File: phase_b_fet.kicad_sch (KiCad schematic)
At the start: 24 parts, among them Q6 IAUS300N08S5N0, Q7 IAUS300N08S5N0, Q8 IAUS300N08S5N0, Q9 IAUS300N08S5N0, U5 INA241A2

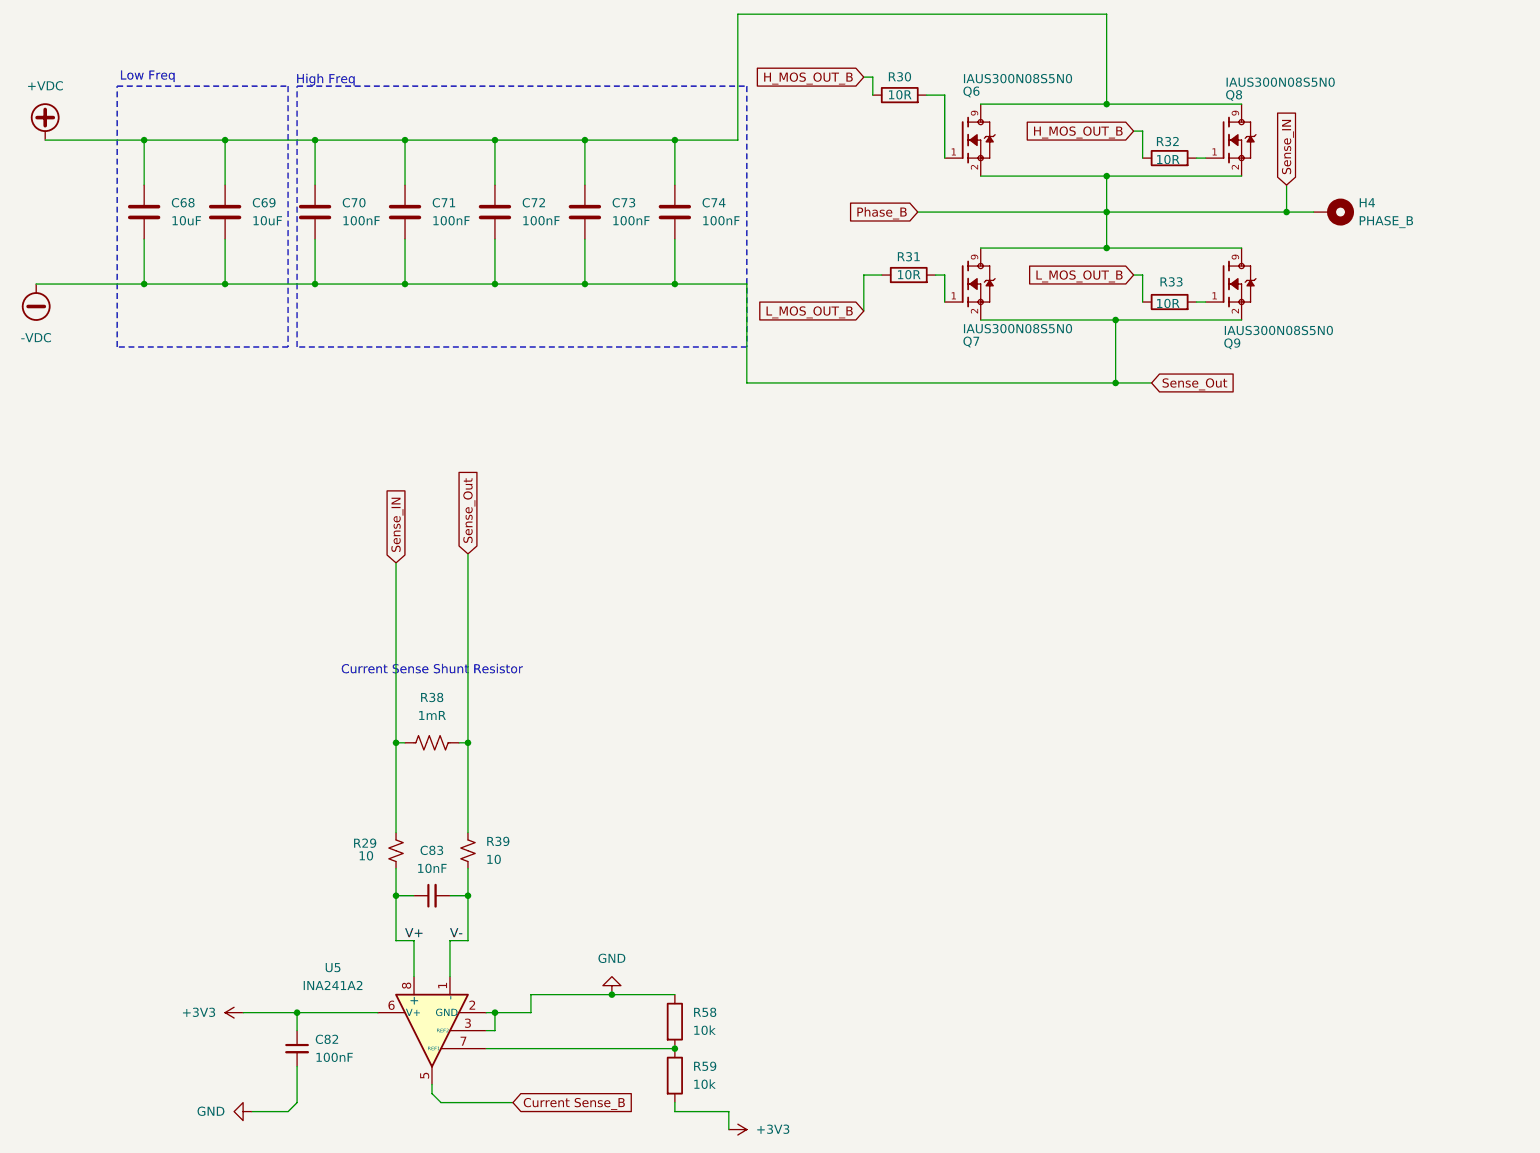
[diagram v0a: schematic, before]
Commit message: update: revised label
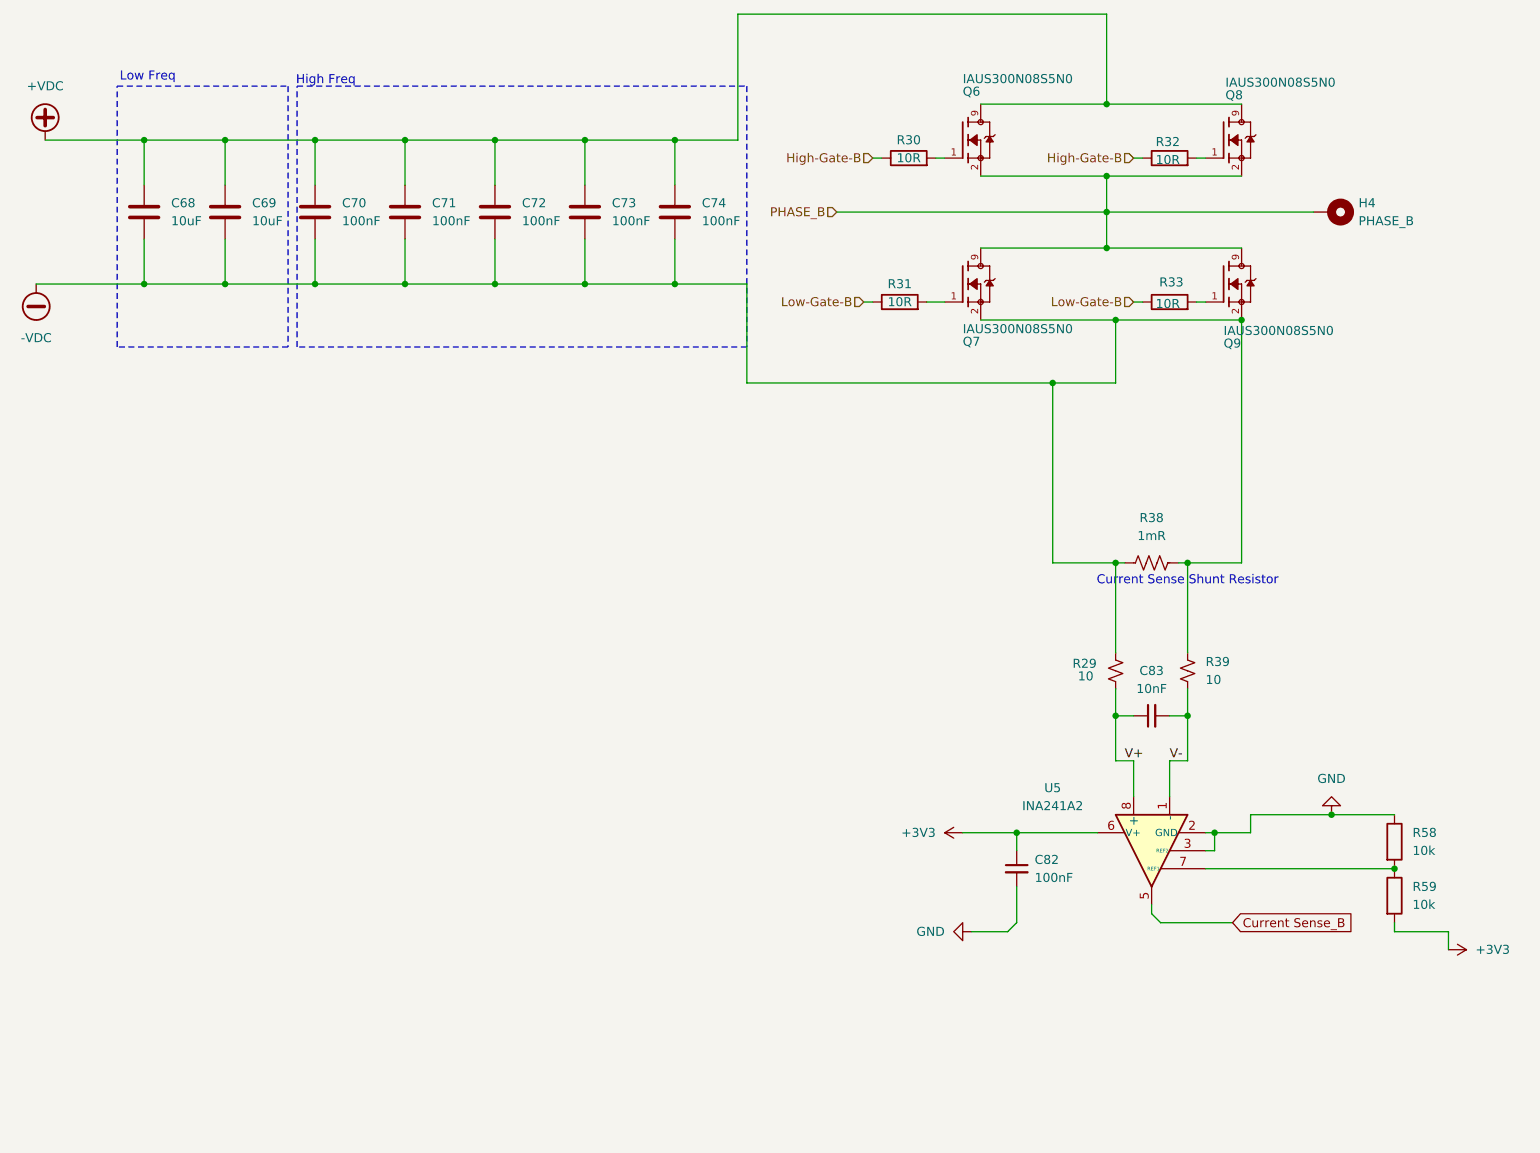
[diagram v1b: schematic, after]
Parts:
- C82, C83: footprint OpenMD:C_0402_1005Metric -> Capacitor_SMD:C_0402_1005Metric_Pad0.74x0.62mm_HandSolder
- R29, R39: footprint OpenMD:R_0402_1005Metric -> Resistor_SMD:R_0402_1005Metric_Pad0.72x0.64mm_HandSolder
- R38: footprint OpenMD:R_2512_6332Metric -> Resistor_SMD:R_2512_6332Metric_Pad1.40x3.35mm_HandSolder
- R58, R59: footprint (none) -> Resistor_SMD:R_1812_4532Metric_Pad1.30x3.40mm_HandSolder
- U5: footprint OpenMD:SOT-23-8 -> Package_TO_SOT_SMD:SOT-23-8_Handsoldering
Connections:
- net -VDC: now also R29.1, R38.1
- net H_MOS_OUT_B renamed High-Gate-B
- net L_MOS_OUT_B renamed Low-Gate-B
- net Phase_B renamed PHASE_B
- net PHASE_B: no longer R29.1, R38.1
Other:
- moved on the sheet: C82, C83, R29, R30, R31, R38, R39, R58, R59, U5

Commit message: LAST I HOPE
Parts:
- added R70: 1mR, Resistor_SMD:R_2512_6332Metric_Pad1.40x3.35mm_HandSolder, symbol OpenMD:R_US
- R58, R59: footprint Resistor_SMD:R_1812_4532Metric_Pad1.30x3.40mm_HandSolder -> Resistor_SMD:R_0603_1608Metric_Pad0.98x0.95mm_HandSolder
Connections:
- net -VDC: now also R70.1, R70.2
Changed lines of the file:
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@@
+	)
+	(junction
+		(at 187.96 114.3)
+		(diameter 0)
+		(color 0 0 0 0)
 	)
 	(junction
@@
 		(color 0 0 0 0)
 	)
+	(junction
+		(at 198.12 114.3)
+		(diameter 0)
+		(color 0 0 0 0)
+	)
 	(wire
 		(pts
@@
 	(wire
 		(pts
+			(xy 196.85 114.3) (xy 198.12 114.3)
+		)
+		(stroke
+			(width 0)
+			(type default)
+		)
+	)
+	(wire
+		(pts
 			(xy 168.91 64.77) (xy 186.69 64.77)
 		)
@@
 	(wire
 		(pts
-			(xy 187.96 109.22) (xy 187.96 121.92)
+			(xy 187.96 109.22) (xy 187.96 114.3)
 		)
 		(stroke
@@
 	(wire
 		(pts
+			(xy 187.96 114.3) (xy 187.96 121.92)
+		)
+		(stroke
+			(width 0)
+			(type default)
+		)
+	)
+	(wire
+		(pts
 			(xy 189.23 109.22) (xy 187.96 109.22)
 		)
@@
 	(wire
 		(pts
+			(xy 198.12 114.3) (xy 198.12 121.92)
+		)
+		(stroke
+			(width 0)
+			(type default)
+		)
+	)
+	(wire
+		(pts
 			(xy 199.39 72.39) (xy 200.66 72.39)
 		)
@@
 	(wire
 		(pts
-			(xy 198.12 109.22) (xy 198.12 121.92)
+			(xy 198.12 109.22) (xy 198.12 114.3)
 		)
 		(stroke
@@
 		(pts
 			(xy 167.64 161.29) (xy 172.72 161.29)
+		)
+		(stroke
+			(width 0)
+			(type default)
+		)
+	)
+	(wire
+		(pts
+			(xy 187.96 114.3) (xy 189.23 114.3)
 		)
 		(stroke
@@
 			)
 		)
-		(property "Footprint" "Resistor_SMD:R_1812_4532Metric_Pad1.30x3.40mm_HandSolder"
+		(property "Footprint" "Resistor_SMD:R_0603_1608Metric_Pad0.98x0.95mm_HandSolder"
 			(at 225.552 148.59 90)
 			(effects
@@
 	)
 	(symbol
+		(lib_id "OpenMD:R_US")
+		(at 193.04 114.3 90)
+		(unit 1)
+		(exclude_from_sim no)
+		(in_bom yes)
+		(on_board yes)
+		(dnp no)
+		(fields_autoplaced yes)
+		(property "Reference" "R70"
+			(at 193.04 107.95 90)
+			(effects
+				(font
+					(size 1.27 1.27)
+				)
+			)
+		)
+		(property "Value" "1mR"
+			(at 193.04 110.49 90)
+			(effects
+				(font
+					(size 1.27 1.27)
+				)
+			)
+		)
+		(property "Footprint" "Resistor_SMD:R_2512_6332Metric_Pad1.40x3.35mm_HandSolder"
+			(at 193.294 113.284 90)
+			(effects
+				(font
+					(size 1.27 1.27)
+				)
+				(hide yes)
+			)
+		)
+		(property "Datasheet" "~"
+			(at 193.04 114.3 0)
+			(effects
+				(font
+					(size 1.27 1.27)
+				)
+				(hide yes)
+			)
+		)
+		(property "Description" "Resistor, US symbol"
+			(at 193.04 114.3 0)
+			(effects
+				(font
+					(size 1.27 1.27)
+				)
+				(hide yes)
+			)
+		)
+		(property "Rating" "3W"
+			(at 193.04 114.3 0)
+			(effects
+				(font
+					(size 1.27 1.27)
+				)
+				(hide yes)
+			)
+		)
+		(property "Source" "LCSC"
+			(at 193.04 114.3 0)
+			(effects
+				(font
+					(size 1.27 1.27)
+				)
+				(hide yes)
+			)
+		)
+		(property "Manufacturer_Part_Number" "ASR-M-3-0.5F"
+			(at 193.04 114.3 0)
+			(effects
+				(font
+					(size 1.27 1.27)
+				)
+				(hide yes)
+			)
+		)
+		(pin "2"
+		)
+		(pin "1"
+		)
+		(instances
+			(project "Motor_Driver_Shell_Eco"
+				(path "/63ef3b9c-05f1-4b00-812a-fede2372efc7/7c8dbef5-e40c-461c-862c-3f756f947d60/9225069e-d350-490c-a3e0-844242190371"
+					(reference "R70")
+					(unit 1)
+				)
+			)
+		)
+	)
+	(symbol
 		(lib_id "OpenMD:C_Small")
 		(at 173.99 152.4 0)
@@
 			)
 		)
-		(property "Footprint" "Resistor_SMD:R_1812_4532Metric_Pad1.30x3.40mm_HandSolder"
+		(property "Footprint" "Resistor_SMD:R_0603_1608Metric_Pad0.98x0.95mm_HandSolder"
 			(at 225.552 156.21 90)
 			(effects

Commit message: rev3
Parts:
- removed H4: PHASE_B, MountingHole:MountingHole_3.7mm_Pad_Via, symbol Mechanical:MountingHole_Pad
- added MP2: Phase_B, WP-BUTR:WP-BUTR_7460307, symbol WP-BUTR:WP-BUTR
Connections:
- net GND is gone; now on net -VDC: C82.2, R58.1, U5.2 (GND), U5.3 (REF2), U5.4 (GND)
- net -VDC: no longer Q7.2, Q7.3, Q7.4, Q7.5, Q7.6, Q7.7, Q7.8, Q9.2, Q9.3, Q9.4, Q9.5, Q9.6, Q9.7, Q9.8, R38.2, R39.1, R70.2
- net PHASE_B: now also MP2.1, MP2.2, MP2.3, MP2.4, MP2.5, MP2.6, MP2.7, MP2.8
- net +3V3 renamed +3V3F
- new net: Q7.2, Q7.3, Q7.4, Q7.5, Q7.6, Q7.7, Q7.8, Q9.2, Q9.3, Q9.4, Q9.5, Q9.6, Q9.7, Q9.8, R38.2, R39.1, R70.2
